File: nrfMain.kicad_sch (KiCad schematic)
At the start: 0 parts

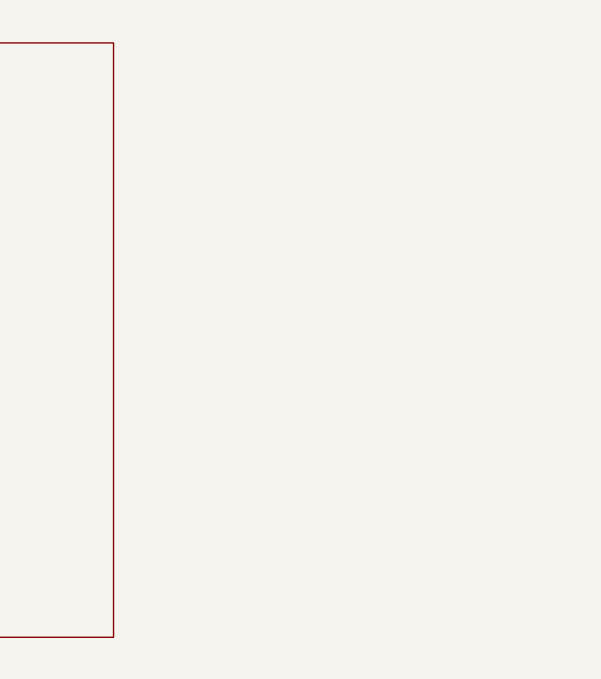
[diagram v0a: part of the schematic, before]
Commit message: Added antenna
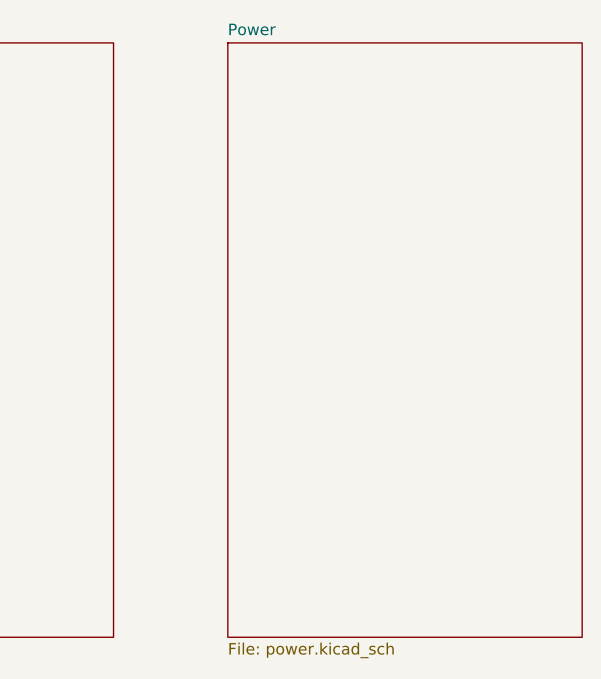
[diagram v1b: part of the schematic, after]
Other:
- added sheet Power (power.kicad_sch)
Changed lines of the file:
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@@
+		)
+	)
+	(sheet
+		(at 140.97 19.05)
+		(size 39.37 66.04)
+		(fields_autoplaced yes)
+		(stroke
+			(width 0.1524)
+			(type solid)
+		)
+		(fill
+			(color 0 0 0 0.0000)
+		)
+		(property "Sheetname" "Power"
+			(at 140.97 18.3384 0)
+			(effects
+				(font
+					(size 1.27 1.27)
+				)
+				(justify left bottom)
+			)
+		)
+		(property "Sheetfile" "power.kicad_sch"
+			(at 140.97 85.6746 0)
+			(effects
+				(font
+					(size 1.27 1.27)
+				)
+				(justify left top)
+			)
+		)
+		(instances
+			(project "nrfMain"
+				(path "/4b478080-1b18-4cae-a6eb-51454cf43595"
+					(page "3")
+				)
+			)
 		)
 	)

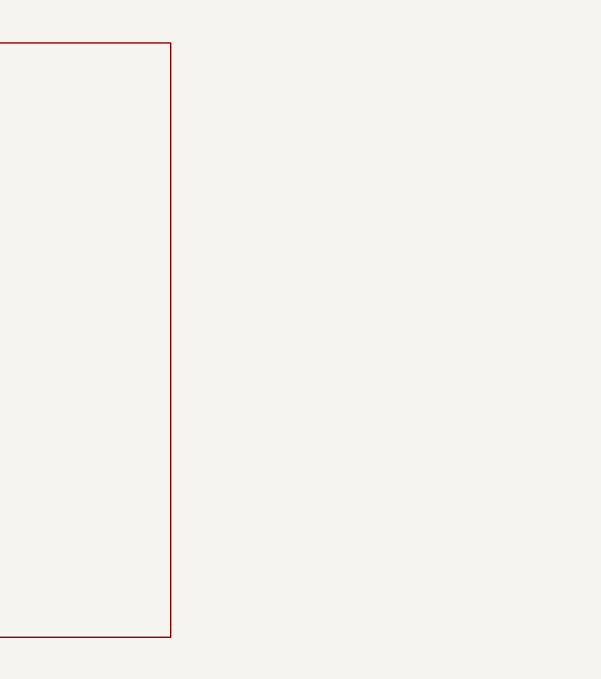
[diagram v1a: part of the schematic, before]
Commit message: Added outputs page
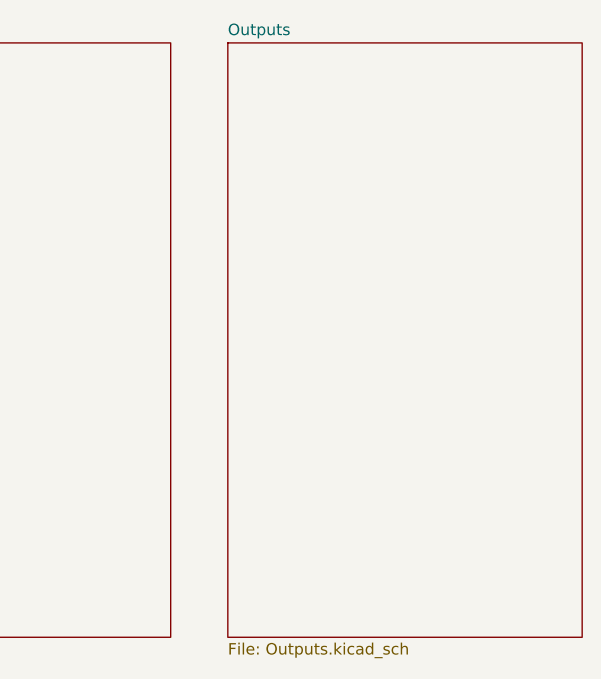
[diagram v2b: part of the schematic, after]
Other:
- added sheet Outputs (Outputs.kicad_sch)
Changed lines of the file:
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@@
+		)
+	)
+	(sheet
+		(at 186.69 19.05)
+		(size 39.37 66.04)
+		(fields_autoplaced yes)
+		(stroke
+			(width 0.1524)
+			(type solid)
+		)
+		(fill
+			(color 0 0 0 0.0000)
+		)
+		(property "Sheetname" "Outputs"
+			(at 186.69 18.3384 0)
+			(effects
+				(font
+					(size 1.27 1.27)
+				)
+				(justify left bottom)
+			)
+		)
+		(property "Sheetfile" "Outputs.kicad_sch"
+			(at 186.69 85.6746 0)
+			(effects
+				(font
+					(size 1.27 1.27)
+				)
+				(justify left top)
+			)
+		)
+		(instances
+			(project "nrfMain"
+				(path "/4b478080-1b18-4cae-a6eb-51454cf43595"
+					(page "4")
+				)
+			)
 		)
 	)

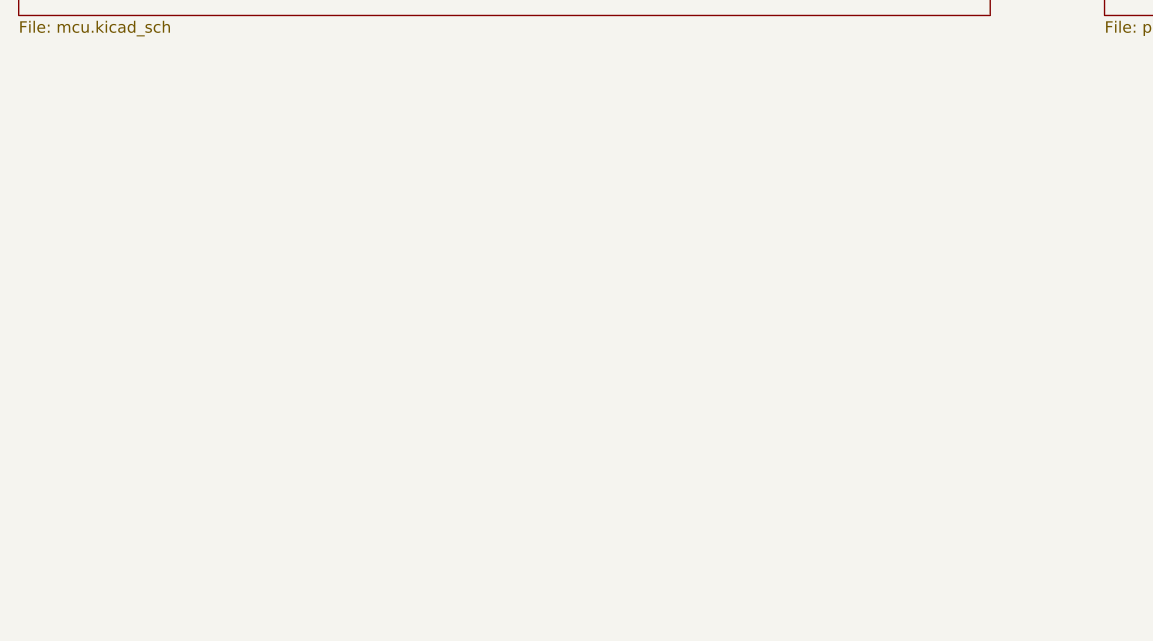
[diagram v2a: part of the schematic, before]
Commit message: Added output headers
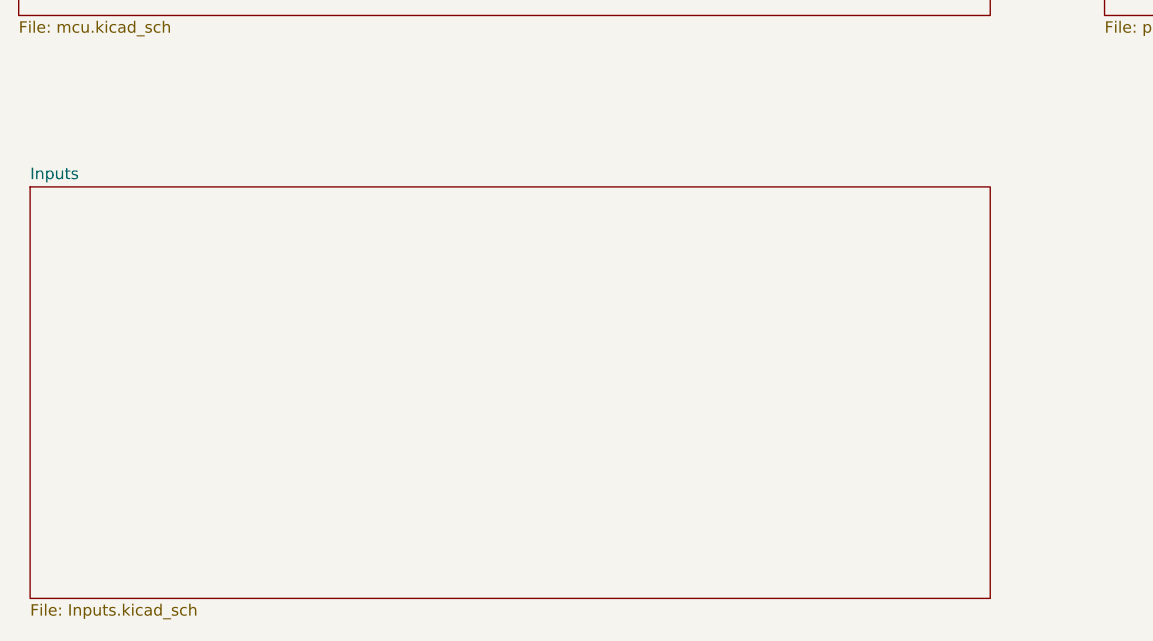
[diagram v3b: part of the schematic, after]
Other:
- added sheet Inputs (Inputs.kicad_sch)
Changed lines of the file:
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@@
+		)
+	)
+	(sheet
+		(at 21.59 104.14)
+		(size 106.68 45.72)
+		(fields_autoplaced yes)
+		(stroke
+			(width 0.1524)
+			(type solid)
+		)
+		(fill
+			(color 0 0 0 0.0000)
+		)
+		(property "Sheetname" "Inputs"
+			(at 21.59 103.4284 0)
+			(effects
+				(font
+					(size 1.27 1.27)
+				)
+				(justify left bottom)
+			)
+		)
+		(property "Sheetfile" "Inputs.kicad_sch"
+			(at 21.59 150.4446 0)
+			(effects
+				(font
+					(size 1.27 1.27)
+				)
+				(justify left top)
+			)
+		)
+		(instances
+			(project "nrfMain"
+				(path "/4b478080-1b18-4cae-a6eb-51454cf43595"
+					(page "5")
+				)
+			)
 		)
 	)

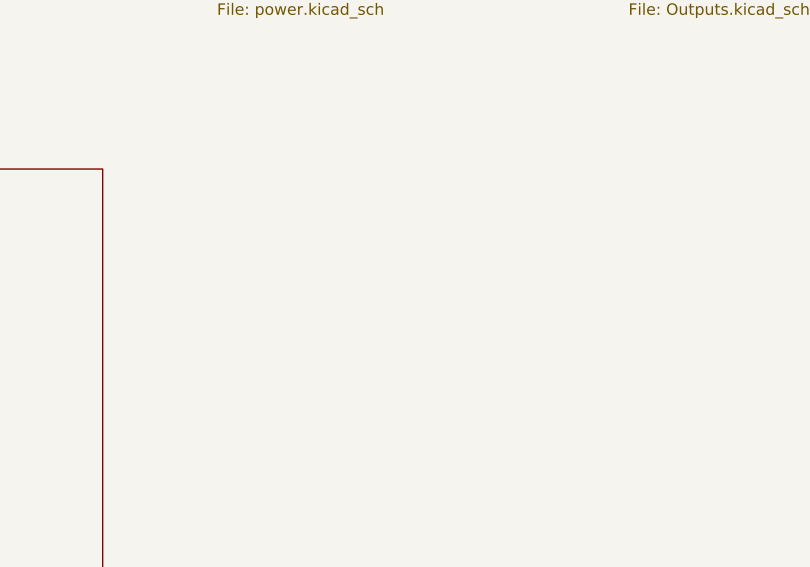
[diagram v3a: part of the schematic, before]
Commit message: Added mounting holes and other final touches
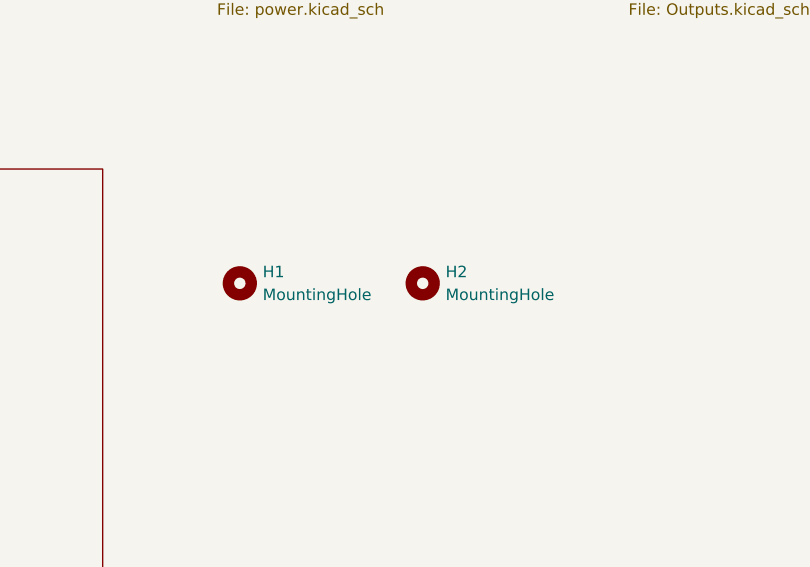
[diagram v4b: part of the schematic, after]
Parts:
- added H1, H2: MountingHole, MountingHole:MountingHole_2.5mm, symbol Mechanical:MountingHole
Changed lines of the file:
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@@
 	(generator_version "8.0")
 	(paper "A4")
+	(symbol
+		(lib_id "Mechanical:MountingHole")
+		(at 143.51 116.84 0)
+		(unit 1)
+		(exclude_from_sim yes)
+		(in_bom no)
+		(on_board yes)
+		(dnp no)
+		(fields_autoplaced yes)
+		(property "Reference" "H1"
+			(at 146.05 115.5699 0)
+			(effects
+				(font
+					(size 1.27 1.27)
+				)
+				(justify left)
+			)
+		)
+		(property "Value" "MountingHole"
+			(at 146.05 118.1099 0)
+			(effects
+				(font
+					(size 1.27 1.27)
+				)
+				(justify left)
+			)
+		)
+		(property "Footprint" "MountingHole:MountingHole_2.5mm"
+			(at 143.51 116.84 0)
+			(effects
+				(font
+					(size 1.27 1.27)
+				)
+				(hide yes)
+			)
+		)
+		(property "Datasheet" "~"
+			(at 143.51 116.84 0)
+			(effects
+				(font
+					(size 1.27 1.27)
+				)
+				(hide yes)
+			)
+		)
+		(property "Description" "Mounting Hole without connection"
+			(at 143.51 116.84 0)
+			(effects
+				(font
+					(size 1.27 1.27)
+				)
+				(hide yes)
+			)
+		)
+		(instances
+			(project ""
+				(path "/4b478080-1b18-4cae-a6eb-51454cf43595"
+					(reference "H1")
+					(unit 1)
+				)
+			)
+		)
+	)
+	(symbol
+		(lib_id "Mechanical:MountingHole")
+		(at 163.83 116.84 0)
+		(unit 1)
+		(exclude_from_sim yes)
+		(in_bom no)
+		(on_board yes)
+		(dnp no)
+		(fields_autoplaced yes)
+		(property "Reference" "H2"
+			(at 166.37 115.5699 0)
+			(effects
+				(font
+					(size 1.27 1.27)
+				)
+				(justify left)
+			)
+		)
+		(property "Value" "MountingHole"
+			(at 166.37 118.1099 0)
+			(effects
+				(font
+					(size 1.27 1.27)
+				)
+				(justify left)
+			)
+		)
+		(property "Footprint" "MountingHole:MountingHole_2.5mm"
+			(at 163.83 116.84 0)
+			(effects
+				(font
+					(size 1.27 1.27)
+				)
+				(hide yes)
+			)
+		)
+		(property "Datasheet" "~"
+			(at 163.83 116.84 0)
+			(effects
+				(font
+					(size 1.27 1.27)
+				)
+				(hide yes)
+			)
+		)
+		(property "Description" "Mounting Hole without connection"
+			(at 163.83 116.84 0)
+			(effects
+				(font
+					(size 1.27 1.27)
+				)
+				(hide yes)
+			)
+		)
+		(instances
+			(project "nrfMain"
+				(path "/4b478080-1b18-4cae-a6eb-51454cf43595"
+					(reference "H2")
+					(unit 1)
+				)
+			)
+		)
+	)
 	(sheet
 		(at 20.32 19.05)
